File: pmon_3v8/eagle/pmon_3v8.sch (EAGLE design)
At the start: 34 parts, among them J1 USB, J2 USB, J4 PINHD-1X3, J5 PINHD-2X3, Q1 16Mhz, U1 LTC2943, U2 FT232RL, U3 LT1764AEQ, U4 ATMEGA328TQFP32

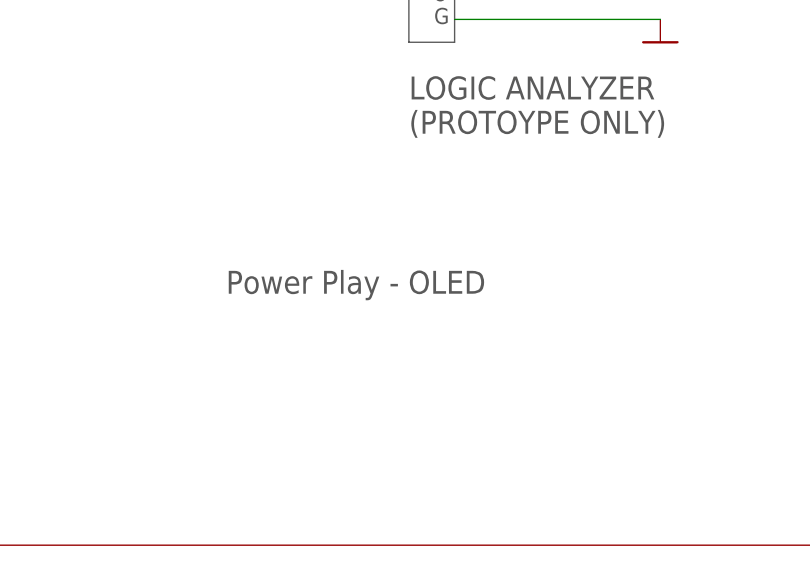
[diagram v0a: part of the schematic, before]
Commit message: Renamed power play oled to power play 3.8V (to be consistent with the 5V name of the other variant).
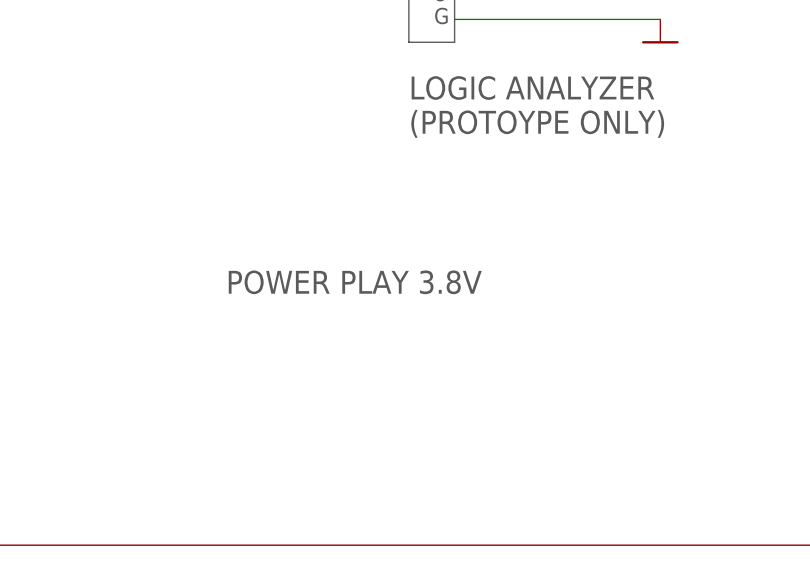
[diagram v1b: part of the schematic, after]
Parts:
- C1, C10, C11, C12, C4, C5, C6, C7, C9: device pmon_oled:CAP-C0603 -> pmon_3v8:CAP-C0603
- C2, C3, C8: device pmon_oled:CPOL-USA/3216-18R -> pmon_3v8:CPOL-USA/3216-18R
- J1, J2: device pmon_oled:USB -> pmon_3v8:USB
- J4: device pmon_oled:PINHD-1X3 -> pmon_3v8:PINHD-1X3
- J5: device pmon_oled:PINHD-2X3 -> pmon_3v8:PINHD-2X3
- OLED: device pmon_oled:OLED -> pmon_3v8:OLED
- Q1: device pmon_oled:CRYSTALCTS406 -> pmon_3v8:CRYSTALCTS406
- R1, R10, R2, R3, R4, R5, R8, R9: device pmon_oled:RES-R0603 -> pmon_3v8:RES-R0603
- R6: device pmon_oled:RES-SHUNT-6432 -> pmon_3v8:RES-SHUNT-6432
- R7: device pmon_oled:TRIM_US-SM-42/43A -> pmon_3v8:TRIM_US-SM-42/43A
- S1: device pmon_oled:PUSH_BUTTON -> pmon_3v8:PUSH_BUTTON
- SB1: device pmon_oled:JUMPER_SOLDER_1X2 -> pmon_3v8:JUMPER_SOLDER_1X2
- U1: device pmon_oled:LTC2943 -> pmon_3v8:LTC2943
- U2: device pmon_oled:FT232RL -> pmon_3v8:FT232RL
- U3: device pmon_oled:LTE1764 -> pmon_3v8:LTE1764
- U4: device pmon_oled:ATMEGA328TQFP32 -> pmon_3v8:ATMEGA328TQFP32
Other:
- note added: "POWER PLAY 3.8V"
- note removed: "Power Play - OLED"

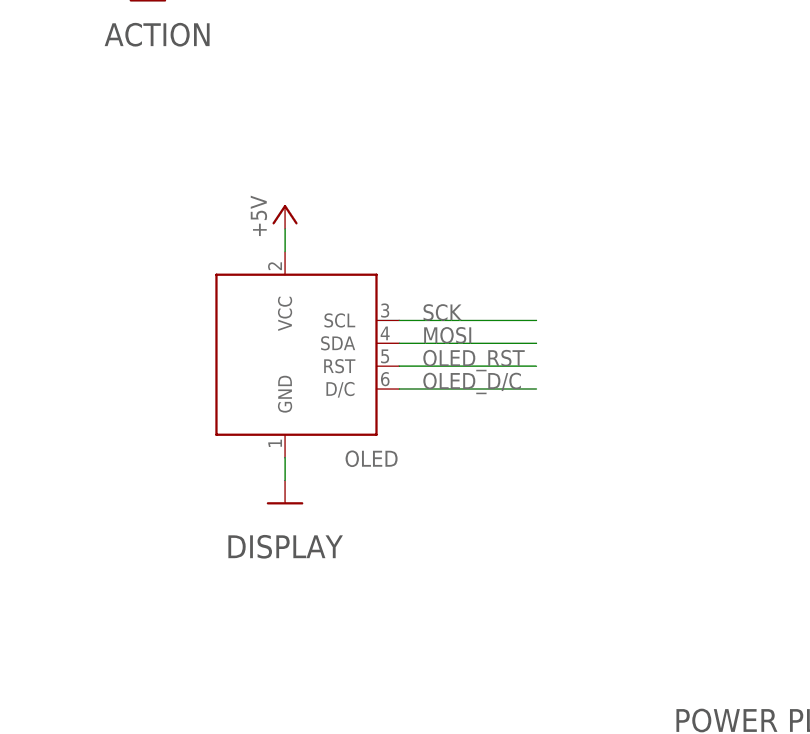
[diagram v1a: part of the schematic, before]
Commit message: Added OLED reset pull down resistor.
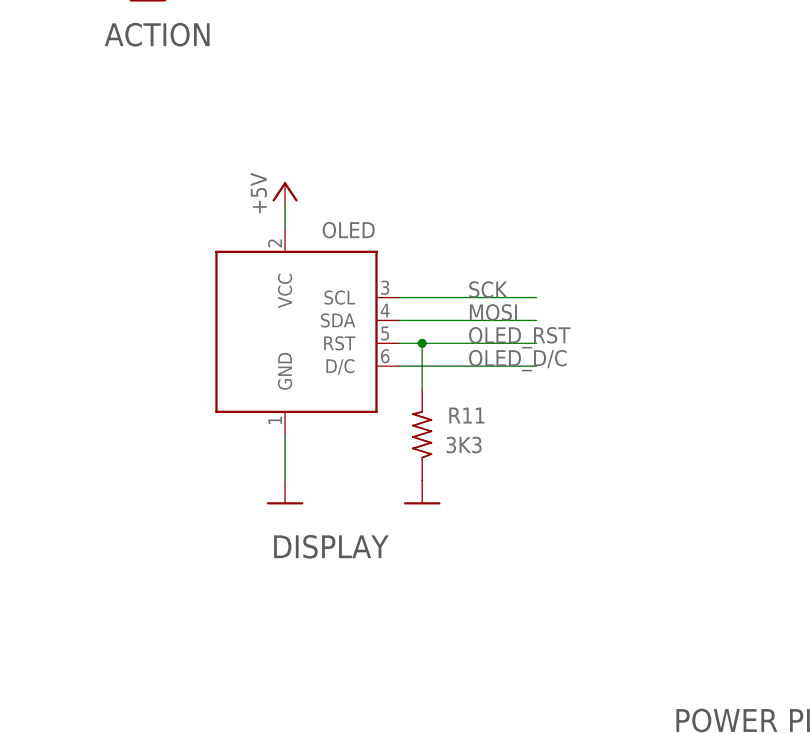
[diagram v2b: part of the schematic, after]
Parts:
- added R11: 3K3, pmon_3v8:RES-R0603
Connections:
- net GND: now also R11.1
- net OLED_RST: now also R11.2
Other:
- moved on the sheet: OLED
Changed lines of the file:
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@@
 <part name="U$18" library="pmon_3v8" deviceset="NC" device=""/>
 <part name="U$19" library="pmon_3v8" deviceset="NC" device=""/>
+<part name="R11" library="pmon_3v8" deviceset="RES-" device="R0603" value="3K3"/>
+<part name="GND2" library="pmon_3v8" deviceset="GND" device=""/>
 </parts>
 <sheets>
@@
 <text x="122.174" y="104.14" size="2.54" layer="97">ACTION</text>
 <text x="-7.112" y="213.106" size="2.54" layer="97">SOURCE</text>
-<text x="135.636" y="47.244" size="2.54" layer="97">DISPLAY</text>
+<text x="140.716" y="47.244" size="2.54" layer="97">DISPLAY</text>
 <text x="78.994" y="57.404" size="2.032" layer="97">Dev</text>
 <text x="273.558" y="7.112" size="2.54" layer="97">C</text>
@@
 <attribute name="VALUE" x="23.876" y="212.852" size="1.778" layer="96"/>
 </instance>
-<instance part="OLED" gate="G$1" x="142.24" y="68.58" smashed="yes">
-<attribute name="NAME" x="148.844" y="57.404" size="1.778" layer="95"/>
+<instance part="OLED" gate="G$1" x="142.24" y="71.12" smashed="yes">
+<attribute name="NAME" x="146.304" y="82.804" size="1.778" layer="95"/>
 </instance>
 <instance part="GND33" gate="1" x="142.24" y="53.34" smashed="yes"/>
-<instance part="P+7" gate="1" x="142.24" y="86.36" smashed="yes" rot="MR0">
-<attribute name="VALUE" x="138.43" y="82.804" size="1.778" layer="96" rot="MR90"/>
+<instance part="P+7" gate="1" x="142.24" y="88.9" smashed="yes" rot="MR0">
+<attribute name="VALUE" x="138.43" y="85.344" size="1.778" layer="96" rot="MR90"/>
 </instance>
 <instance part="U$9" gate="G$1" x="238.76" y="162.56" rot="R180"/>
@@
 <instance part="U$18" gate="G$1" x="238.76" y="210.82" rot="R180"/>
 <instance part="U$19" gate="G$1" x="238.76" y="213.36" rot="R180"/>
+<instance part="R11" gate="G$1" x="157.48" y="60.96" smashed="yes" rot="MR90">
+<attribute name="NAME" x="160.274" y="62.2046" size="1.778" layer="95"/>
+<attribute name="VALUE" x="160.02" y="58.928" size="1.778" layer="96"/>
+</instance>
+<instance part="GND2" gate="1" x="157.48" y="53.34" smashed="yes"/>
 </instances>
 <busses>
@@
 <segment>
 <pinref part="OLED" gate="G$1" pin="GND"/>
-<wire x1="142.24" y1="58.42" x2="142.24" y2="55.88" width="0.1524" layer="91"/>
+<wire x1="142.24" y1="60.96" x2="142.24" y2="55.88" width="0.1524" layer="91"/>
 <pinref part="GND33" gate="1" pin="GND"/>
+</segment>
+<segment>
+<pinref part="R11" gate="G$1" pin="1"/>
+<pinref part="GND2" gate="1" pin="GND"/>
 </segment>
 </net>
@@
 <segment>
 <pinref part="OLED" gate="G$1" pin="VCC"/>
-<wire x1="142.24" y1="81.28" x2="142.24" y2="83.82" width="0.1524" layer="91"/>
+<wire x1="142.24" y1="83.82" x2="142.24" y2="86.36" width="0.1524" layer="91"/>
 <pinref part="P+7" gate="1" pin="+5V"/>
 </segment>
@@
 <segment>
 <pinref part="OLED" gate="G$1" pin="SCL"/>
-<wire x1="154.94" y1="73.66" x2="170.18" y2="73.66" width="0.1524" layer="91"/>
-<label x="157.48" y="73.66" size="1.778" layer="95"/>
+<wire x1="154.94" y1="76.2" x2="170.18" y2="76.2" width="0.1524" layer="91"/>
+<label x="162.56" y="76.2" size="1.778" layer="95"/>
 </segment>
 <segment>
@@
 <segment>
 <pinref part="OLED" gate="G$1" pin="SDA"/>
-<wire x1="154.94" y1="71.12" x2="170.18" y2="71.12" width="0.1524" layer="91"/>
-<label x="157.48" y="71.12" size="1.778" layer="95"/>
+<wire x1="154.94" y1="73.66" x2="170.18" y2="73.66" width="0.1524" layer="91"/>
+<label x="162.56" y="73.66" size="1.778" layer="95"/>
 </segment>
 <segment>
@@
 <segment>
 <pinref part="OLED" gate="G$1" pin="D/C"/>
-<wire x1="154.94" y1="66.04" x2="170.18" y2="66.04" width="0.1524" layer="91"/>
-<label x="157.48" y="66.04" size="1.778" layer="95"/>
+<wire x1="154.94" y1="68.58" x2="170.18" y2="68.58" width="0.1524" layer="91"/>
+<label x="162.56" y="68.58" size="1.778" layer="95"/>
 </segment>
 </net>
@@
 <segment>
 <pinref part="OLED" gate="G$1" pin="RST"/>
-<wire x1="154.94" y1="68.58" x2="170.18" y2="68.58" width="0.1524" layer="91"/>
-<label x="157.48" y="68.58" size="1.778" layer="95"/>
-</segment>
-</net>
+<wire x1="154.94" y1="71.12" x2="157.48" y2="71.12" width="0.1524" layer="91"/>
+<label x="162.56" y="71.12" size="1.778" layer="95"/>
+<pinref part="R11" gate="G$1" pin="2"/>
+<wire x1="157.48" y1="71.12" x2="170.18" y2="71.12" width="0.1524" layer="91"/>
+<wire x1="157.48" y1="66.04" x2="157.48" y2="71.12" width="0.1524" layer="91"/>
+<junction x="157.48" y="71.12"/>
+</segment>
+</net>

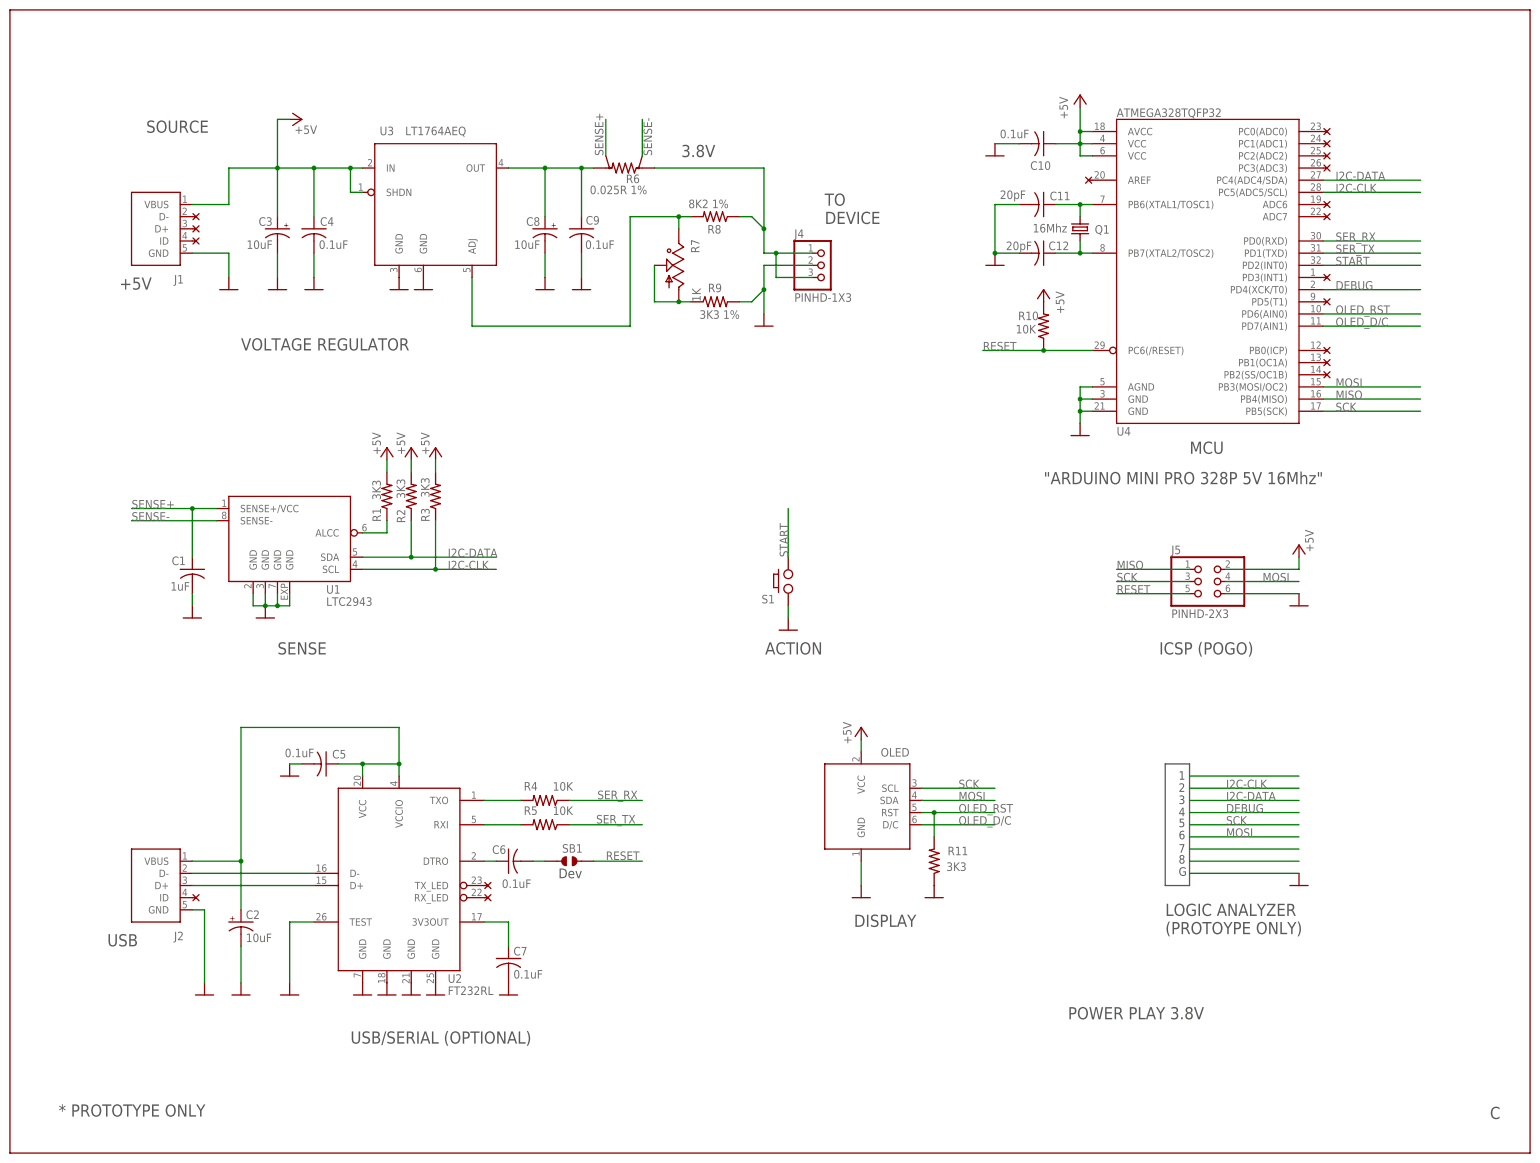
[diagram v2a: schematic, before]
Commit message: Added 4V regulator. Yet to do final auto routing.
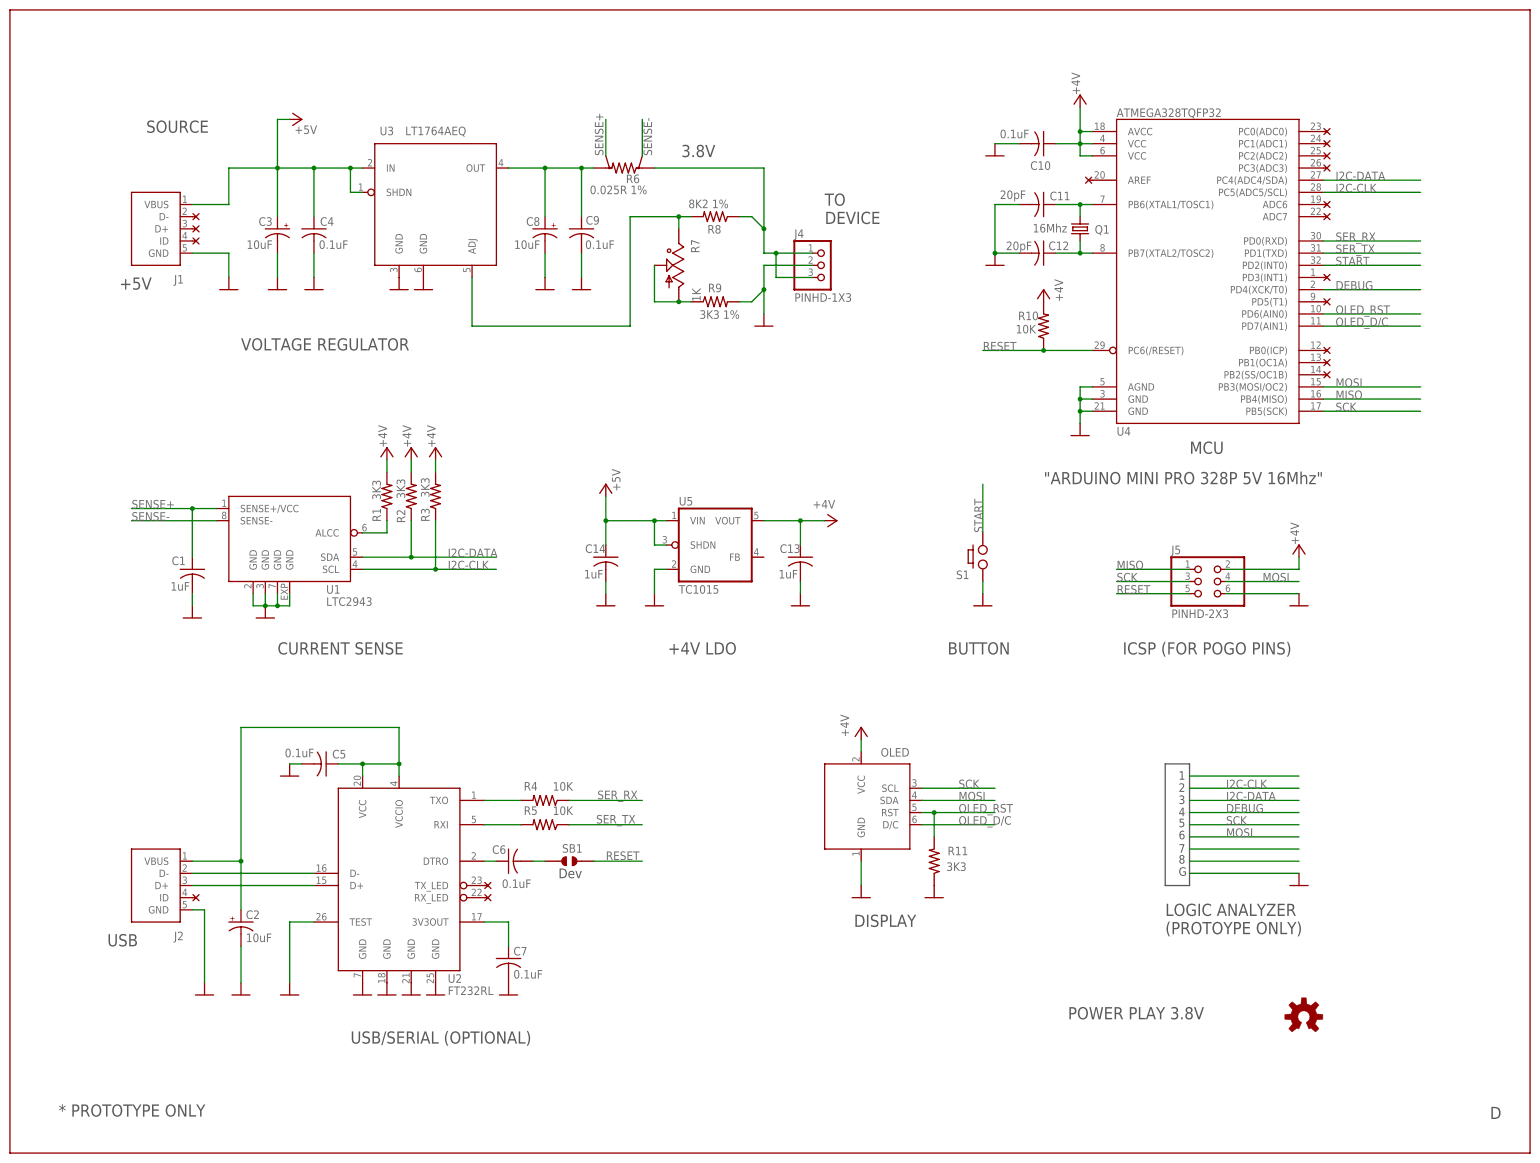
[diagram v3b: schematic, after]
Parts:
- added C13, C14: 1uF, pmon_3v8:CAP-C0603
- added U$28: OSH, pmon_3v8:OSH
- added U5: TC1015, pmon_3v8:TC1015
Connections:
- new net +4V: C10.1, C13.1, J5.2, OLED.VCC, R1.2, R10.2, R2.2, R3.2, U4.AVCC, U4.VCC@1, U4.VCC@2, U5.VOUT
- net +5V: now also C14.1, U5.SHDN, U5.VIN; no longer C10.1, J5.2, OLED.VCC, R1.2, R10.2, R2.2, R3.2, U4.AVCC, U4.VCC@1, U4.VCC@2
- net GND: now also C13.2, C14.2, U5.GND
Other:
- note added: "+4V LDO"
- note added: "BUTTON"
- note added: "CURRENT SENSE"
- note added: "D"
- note added: "ICSP (FOR POGO PINS)"
- note removed: "ACTION"
- note removed: "C"
- note removed: "ICSP (POGO)"
- note removed: "SENSE"
- moved on the sheet: S1
